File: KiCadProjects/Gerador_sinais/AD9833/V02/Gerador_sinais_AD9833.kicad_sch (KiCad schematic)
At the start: 19 parts, among them J1 alimentacao analogica, J2 sinais analogicos, J3 comunicacao / sinais digitais, J4 Conn_01x07, U1 AD828AN, U2 X9c10x, U3 AD9833_module

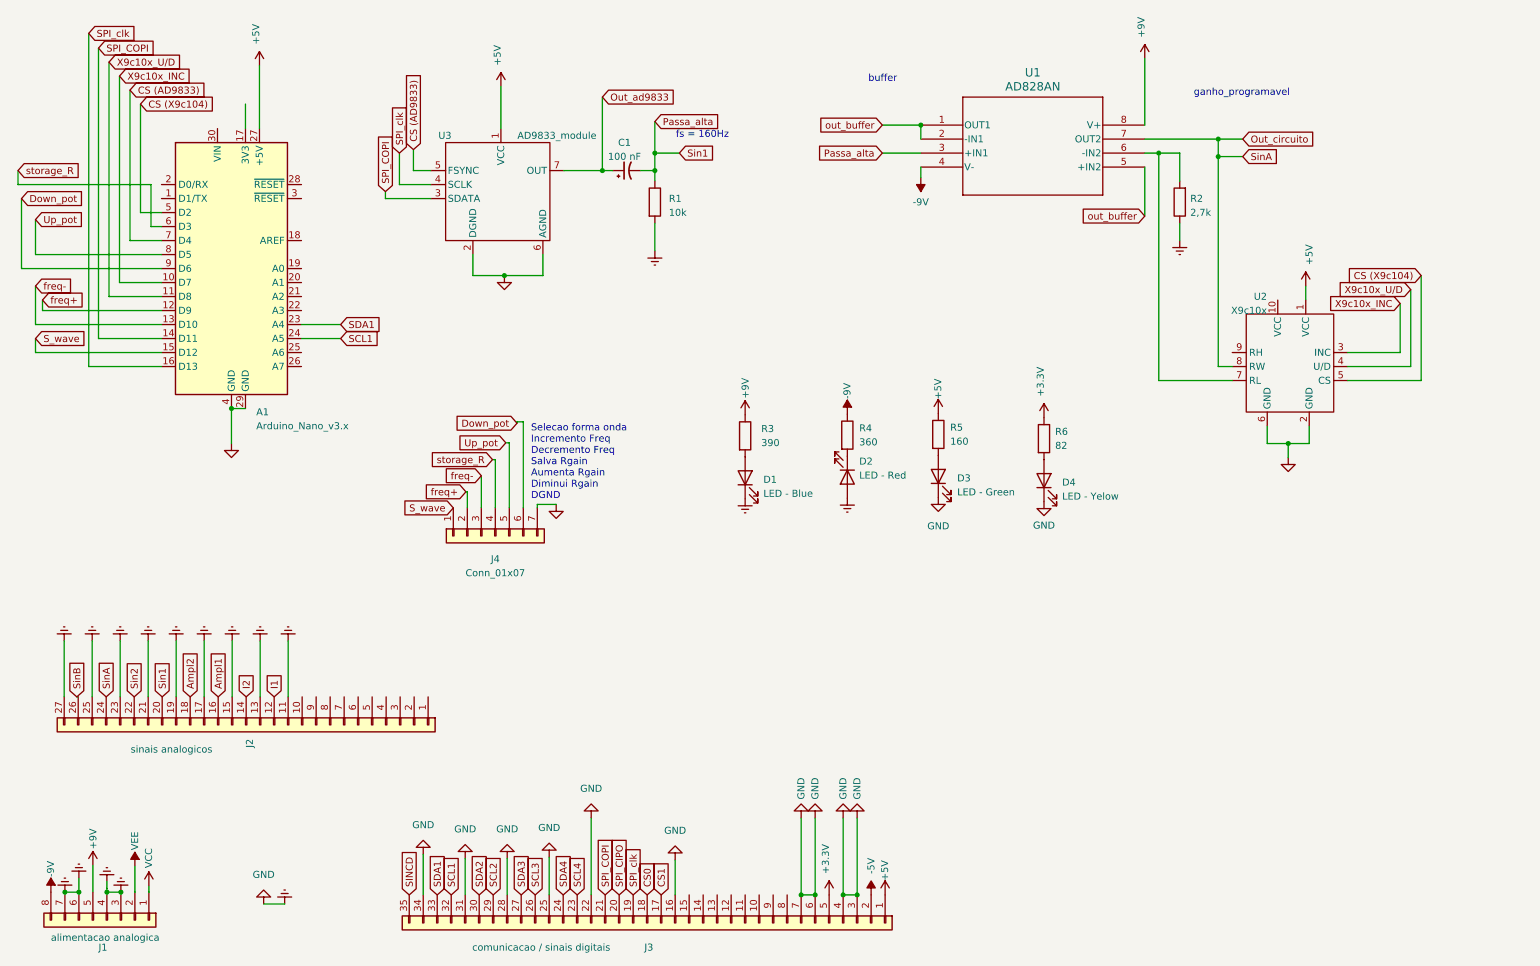
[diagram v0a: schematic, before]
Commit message: mudança AmpOp n inversor
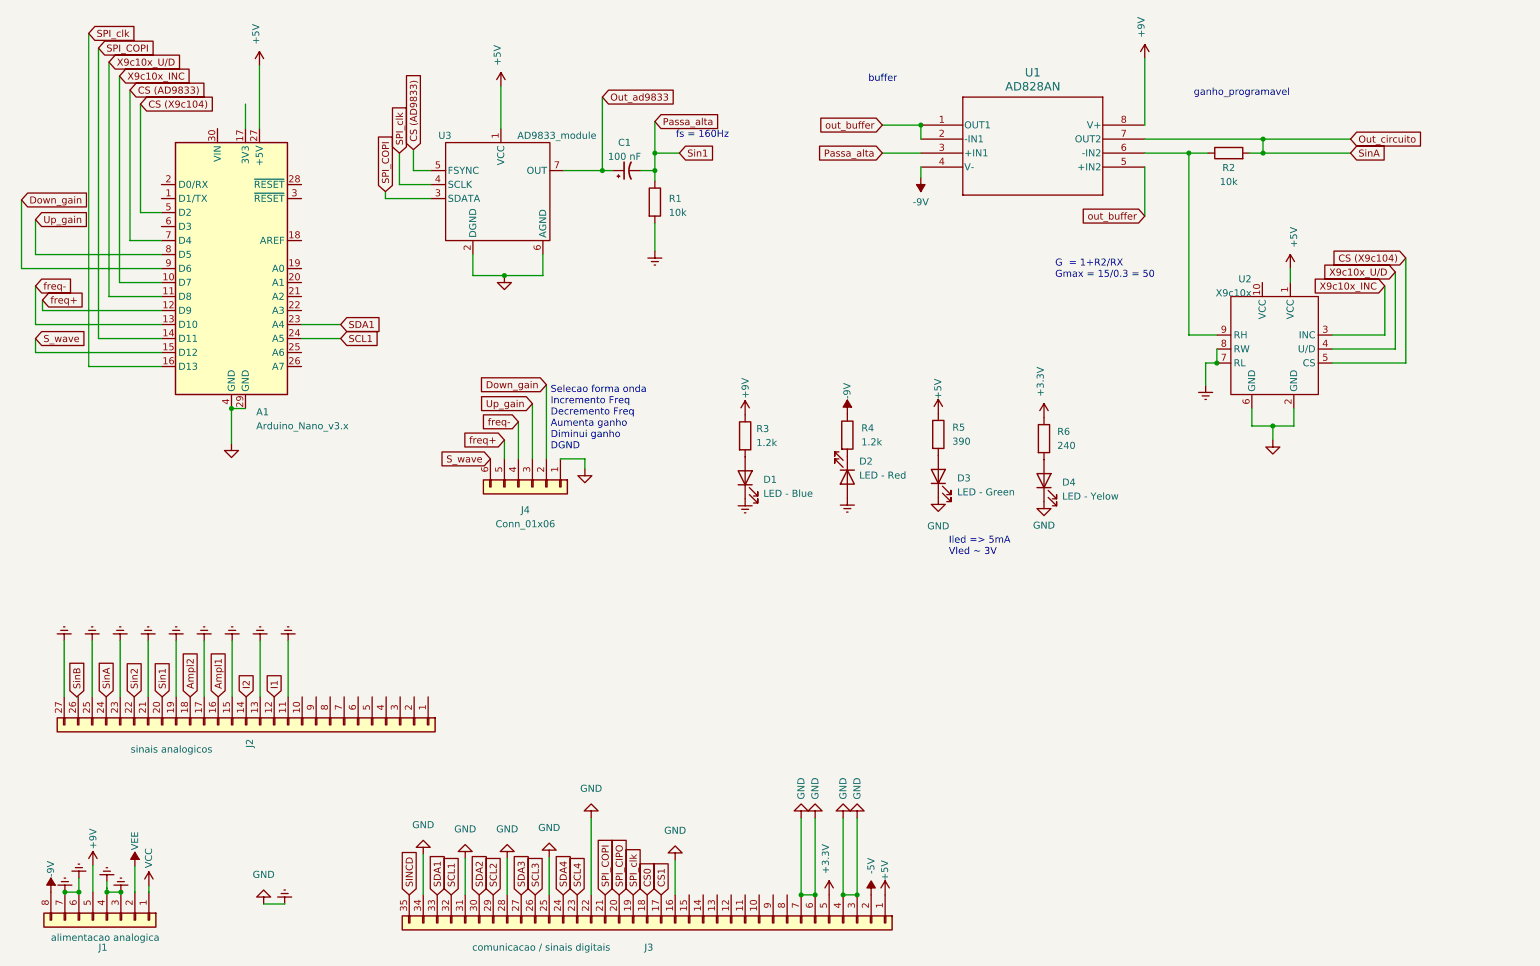
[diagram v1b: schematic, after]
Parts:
- removed J4: Conn_01x07, Connector_PinHeader_2.54mm:PinHeader_1x07_P2.54mm_Horizontal, symbol Connector_Generic:Conn_01x07
- added J4: Conn_01x06, Connector_PinHeader_2.54mm:PinHeader_1x06_P2.54mm_Vertical, symbol Connector_Generic:Conn_01x06
- R2: value 2,7k -> 10k; footprint Resistor_THT:R_Axial_DIN0204_L3.6mm_D1.6mm_P5.08mm_Horizontal -> Resistor_THT:R_Axial_DIN0207_L6.3mm_D2.5mm_P7.62mm_Horizontal
- R3: value 390 -> 1.2k
- R4: value 360 -> 1.2k
- R5: value 160 -> 390
- R6: value 82 -> 240
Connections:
- net Earth: now also U2.7 (RL), U2.8 (RW), J4.1 (Pin_1); no longer R2.1
- net Out_circuito: now also R2.2; no longer U2.8 (RW)
- net S_wave: now also J4.6 (Pin_6)
- net freq+: now also J4.5 (Pin_5)
- net freq-: now also J4.4 (Pin_4)
- net at U2.9 (RH): now also R2.1, U1.6 (-IN2)
- net Down_pot renamed Down_gain
- net Down_gain: now also J4.2 (Pin_2)
- net Up_pot renamed Up_gain
- net Up_gain: now also J4.3 (Pin_3)
- net storage_R: no longer names the net of A1.6 (D3)
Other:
- note added: "G = 1+R2/RX Gmax = 15/0.3 = 50"
- note added: "Iled => 5mA Vled ~ 3V"
- note added: "Selecao forma onda Incremento Freq Decremento Freq Aumenta ganho Diminui ganho DGND"
- note removed: "Selecao forma onda Incremento Freq Decremento Freq Salva Rgain Aumenta Rgain Diminui Rgain DGND"
- moved on the sheet: U2

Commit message: mudanca freq corte
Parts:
- D1: value LED - Blue -> LED Blue
- D2: value LED - Red -> LED Red
- D3: value LED - Green -> LED Green
- R1: value 10k -> 160k
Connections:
- net SPI_COPI: no longer A1.14 (D11), U3.3 (SDATA)
- net SPI_clk: no longer A1.16 (D13), U3.4 (SCLK)
- new net SPI_COPI  (AD9833): A1.14 (D11), U3.3 (SDATA)
- new net SPI_clk  (AD9833): A1.16 (D13), U3.4 (SCLK)
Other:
- note added: "fc = 10Hz"
- note removed: "fs = 160Hz"

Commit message: Baseado barramento v04 - Finalizado - implementacao resistor pullup i2c 2
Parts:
- removed U2: X9c10x, X9c10X_module:X9c10X_module, symbol X9c10X_module:X9c10X_module
- added C2: 100nF, Capacitor_THT:C_Disc_D3.0mm_W1.6mm_P2.50mm, symbol Device:C
- added J5: Select SinA, Connector_PinHeader_2.54mm:PinHeader_1x03_P2.54mm_Vertical, symbol Connector_Generic:Conn_01x03
- added R9: 160k, Resistor_THT:R_Axial_DIN0207_L6.3mm_D2.5mm_P7.62mm_Horizontal, symbol Device:R
- added RpSCL1, RpSDA1: 4k7, Resistor_THT:R_Axial_DIN0207_L6.3mm_D2.5mm_P7.62mm_Horizontal, symbol Device:R
- added U2-DigPot1: X9c10x, X9c10X_module:X9c10X_module, symbol X9c10X_module:X9c10X_module
- J4: value Conn_01x06 -> botoes_selecao
- renumbered D4 to L+3.3v1, D3 to L+5v1, D1 to L+9v1, D2 to L-9v1, U1 to U1-ganho1
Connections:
- net +3.3V: now also RpSCL1.2, RpSDA1.2
- net +5V: now also U2-DigPot1.1 (VCC), U2-DigPot1.10 (VCC)
- net CS (X9c104): now also U2-DigPot1.5 (CS)
- net Earth: now also U1-ganho1.3 (+IN1), R9.2, U2-DigPot1.2 (GND), U2-DigPot1.6 (GND)
- net SCL1: now also RpSCL1.1
- net SDA1: now also RpSDA1.1
- net X9c10x_INC: now also U2-DigPot1.3 (INC)
- net X9c10x_U/D: now also U2-DigPot1.4 (U/D)
- net at R2.1: now also U1-ganho1.2 (-IN1), U2-DigPot1.8 (RW), U2-DigPot1.9 (RH); no longer U1-ganho1.6 (-IN2)
- removed net Out_circuito: J2.24 (Pin_24), R2.2, U1-ganho1.7 (OUT2)
- net Passa_alta renamed Sin1
- net Sin1: now also U1-ganho1.5 (+IN2); no longer U1-ganho1.3 (+IN1)
- removed net out_buffer: U1-ganho1.1 (OUT1), U1-ganho1.2 (-IN1), U1-ganho1.5 (+IN2)
- new net OutBuffer: U1-ganho1.6 (-IN2), U1-ganho1.7 (OUT2), U2-DigPot1.7 (RL)
- new net Sin1_filter: C2.2, J5.1 (Pin_1), R9.1
- new net Sin1_gain: C2.1, J5.3 (Pin_3), R2.2, U1-ganho1.1 (OUT1)
- new net SinA: J2.24 (Pin_24), J5.2 (Pin_2)
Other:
- note added: "Selecao de sinais: Sinal pós ganho Sinal pós ganho + PA"
- note removed: "G = 1+R2/RX Gmax = 15/0.3 = 50"
- moved on the sheet: U1-ganho1

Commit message: temp
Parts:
- removed RpSCL1, RpSDA1: 4k7, Resistor_THT:R_Axial_DIN0207_L6.3mm_D2.5mm_P7.62mm_Horizontal, symbol Device:R
- added J6: Encoder KY-040, Connector_PinHeader_2.54mm:PinHeader_1x05_P2.54mm_Vertical, symbol Connector_Generic:Conn_01x05
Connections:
- net +5V: now also J6.4 (Pin_4)
- net Earth: now also J6.5 (Pin_5)
- net SCL1: no longer A1.24 (A5)
- net SDA1: no longer A1.23 (A4)
- net S_wave renamed En3
- net En3: now also J6.3 (Pin_3)
- net freq+ renamed En2
- net En2: now also J6.2 (Pin_2)
- net freq- renamed En1
- net En1: now also J6.1 (Pin_1)
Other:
- moved on the sheet: J4, L+3.3v1, L+5v1, L+9v1, L-9v1, R3, R4, R5, R6
